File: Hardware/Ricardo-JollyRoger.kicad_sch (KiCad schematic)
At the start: 46 parts, among them J1 RBUS, J3 Conn_01x08_Pin, U1 ESP32-S3, U7 LM66200DRLR, Y1 R940000171

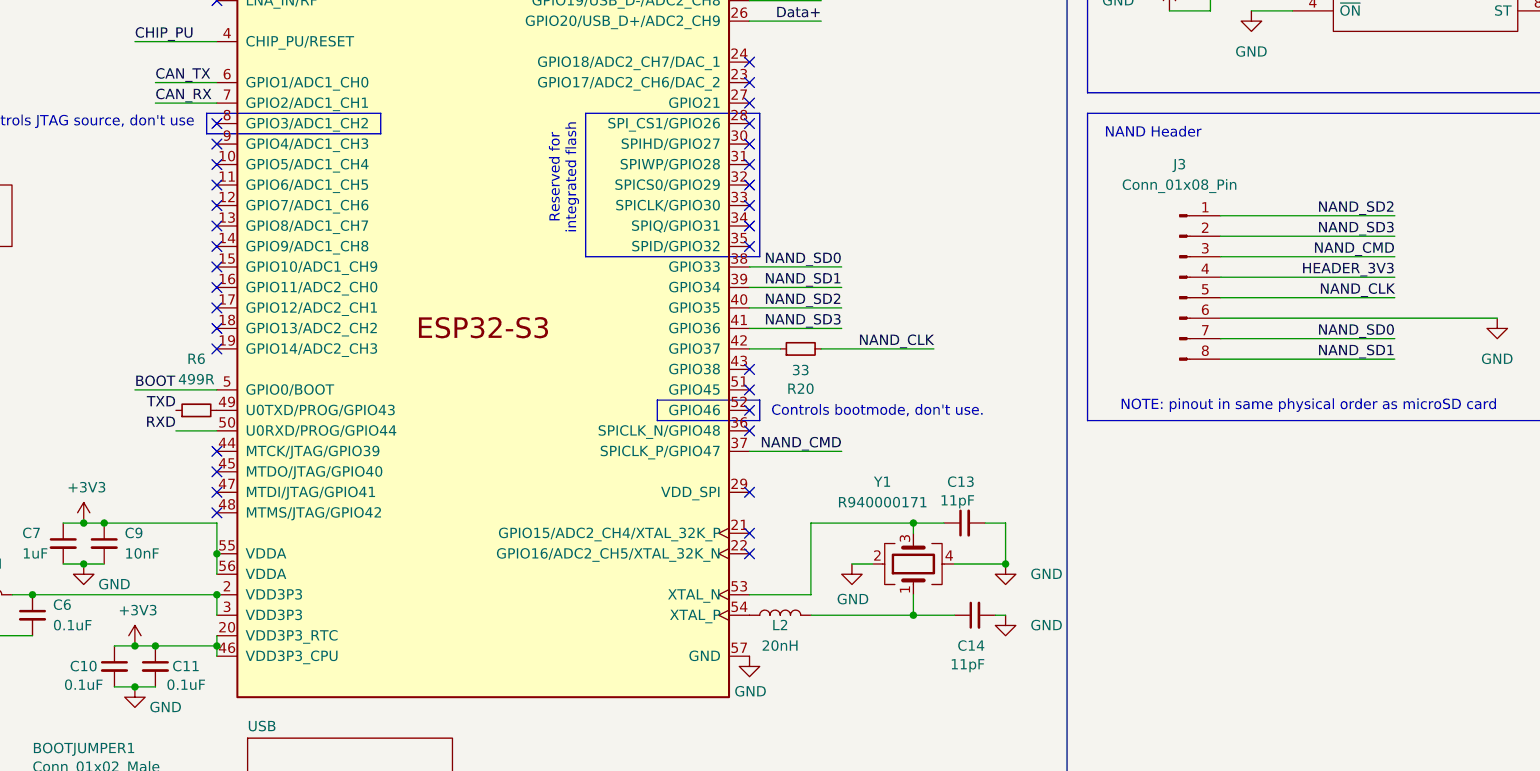
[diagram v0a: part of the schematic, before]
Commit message: Added GPIO breakout
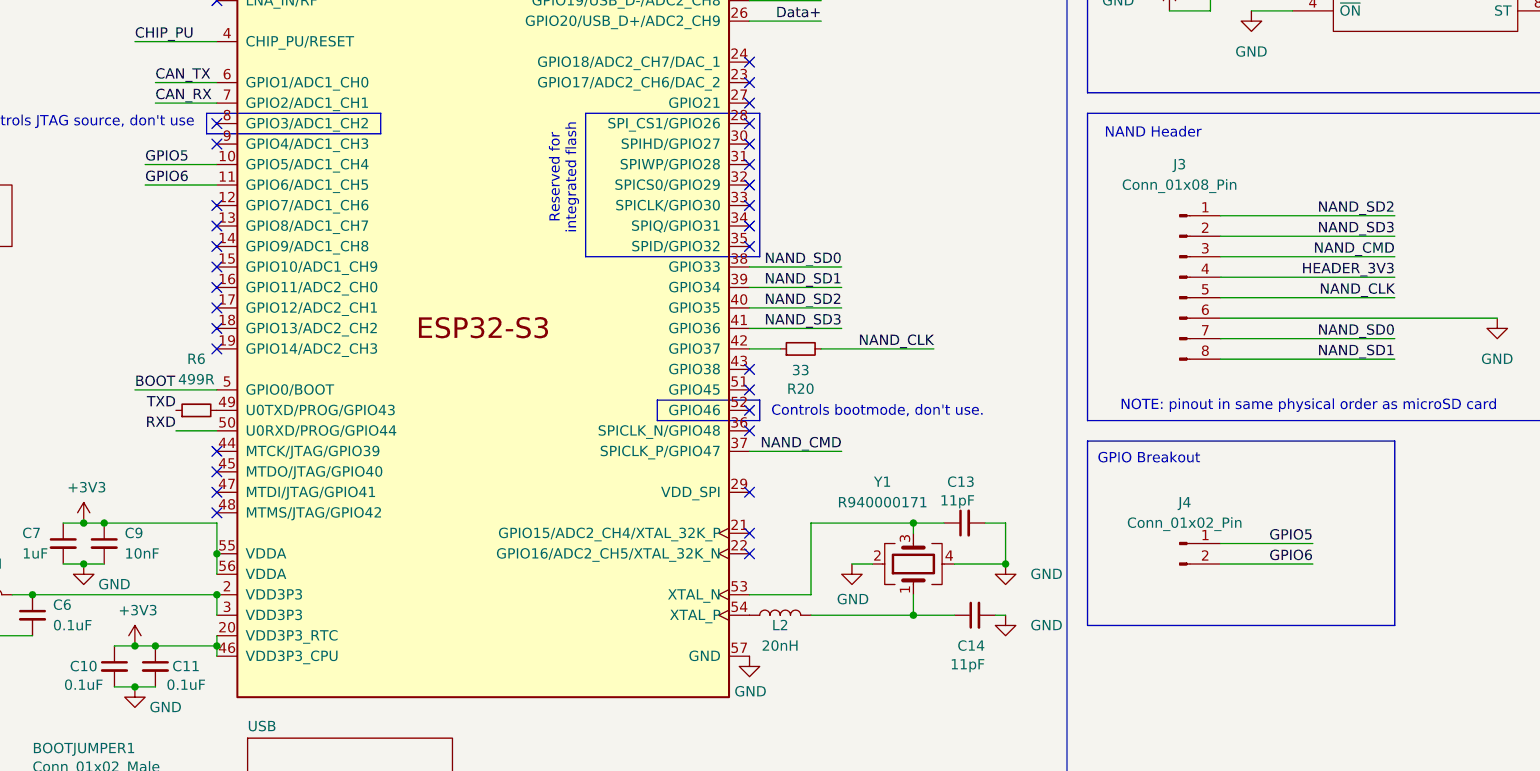
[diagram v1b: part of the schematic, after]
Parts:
- added J4: Conn_01x02_Pin, Connector_Molex:Molex_Pico-Clasp_202396-0207_1x02-1MP_P1.00mm_Horizontal, symbol Connector:Conn_01x02_Pin
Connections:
- net GPIO5: now reaches U1.10 (GPIO5/ADC1_CH4)
- net GPIO5: now also J4.1 (Pin_1)
- net GPIO6: now reaches U1.11 (GPIO6/ADC1_CH5)
- net GPIO6: now also J4.2 (Pin_2)
- no-connect marks 34 -> 32
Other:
- note added: "GPIO Breakout"
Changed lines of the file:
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@@
 	)
 	(no_connect
-		(at 69.85 82.55)
-	)
-	(no_connect
 		(at 135.89 87.63)
 	)
@@
 	)
 	(no_connect
-		(at 69.85 85.09)
-	)
-	(no_connect
 		(at 135.89 72.39)
 	)
@@
 	(wire
 		(pts
+			(xy 60.96 82.55) (xy 69.85 82.55)
+		)
+		(stroke
+			(width 0)
+			(type default)
+		)
+	)
+	(wire
+		(pts
 			(xy 30.48 182.88) (xy 30.48 185.42)
 		)
@@
 	(wire
 		(pts
+			(xy 60.96 85.09) (xy 69.85 85.09)
+		)
+		(stroke
+			(width 0)
+			(type default)
+		)
+	)
+	(wire
+		(pts
 			(xy 156.21 127) (xy 156.21 128.27)
 		)
@@
 		)
 	)
+	(wire
+		(pts
+			(xy 194.31 129.54) (xy 205.74 129.54)
+		)
+		(stroke
+			(width 0)
+			(type default)
+		)
+	)
 	(polyline
 		(pts
@@
 	(wire
 		(pts
+			(xy 194.31 132.08) (xy 205.74 132.08)
+		)
+		(stroke
+			(width 0)
+			(type default)
+		)
+	)
+	(wire
+		(pts
 			(xy 13.97 40.64) (xy 22.86 40.64)
 		)
@@
 		)
 	)
+	(rectangle
+		(start 177.8 116.84)
+		(end 215.9 139.7)
+		(stroke
+			(width 0)
+			(type default)
+		)
+		(fill
+			(type none)
+		)
+	)
 	(text "Controls bootmode, don't use.\n"
 		(exclude_from_sim no)
@@
 		)
 	)
+	(text "GPIO Breakout"
+		(exclude_from_sim no)
+		(at 185.42 119.126 0)
+		(effects
+			(font
+				(size 1.27 1.27)
+			)
+		)
+	)
 	(text "Controls JTAG source, don't use\n"
 		(exclude_from_sim no)
@@
 		)
 	)
+	(label "GPIO6"
+		(at 205.74 132.08 180)
+		(fields_autoplaced yes)
+		(effects
+			(font
+				(size 1.27 1.27)
+			)
+			(justify right bottom)
+		)
+	)
 	(label "CAN_TX"
 		(at 13.97 30.48 0)
@@
 		)
 	)
+	(label "GPIO5"
+		(at 60.96 82.55 0)
+		(fields_autoplaced yes)
+		(effects
+			(font
+				(size 1.27 1.27)
+			)
+			(justify left bottom)
+		)
+	)
 	(label "NAND_SD0"
 		(at 222.25 31.75 180)
@@
 		)
 	)
+	(label "GPIO5"
+		(at 205.74 129.54 180)
+		(fields_autoplaced yes)
+		(effects
+			(font
+				(size 1.27 1.27)
+			)
+			(justify right bottom)
+		)
+	)
 	(label "CAN-"
 		(at 115.57 187.96 0)
@@
 		)
 	)
+	(label "GPIO6"
+		(at 60.96 85.09 0)
+		(fields_autoplaced yes)
+		(effects
+			(font
+				(size 1.27 1.27)
+			)
+			(justify left bottom)
+		)
+	)
 	(label "TXD"
 		(at 17.78 21.59 0)
@@
 					(unit 1)
 				)
+			)
+		)
+	)
+	(symbol
+		(lib_id "Connector:Conn_01x02_Pin")
+		(at 189.23 129.54 0)
+		(unit 1)
+		(exclude_from_sim no)
+		(in_bom yes)
+		(on_board yes)
+		(dnp no)
+		(fields_autoplaced yes)
+		(property "Reference" "J4"
+			(at 189.865 124.46 0)
+			(effects
+				(font
+					(size 1.27 1.27)
+				)
+			)
+		)
+		(property "Value" "Conn_01x02_Pin"
+			(at 189.865 127 0)
+			(effects
+				(font
+					(size 1.27 1.27)
+				)
+			)
+		)
+		(property "Footprint" "Connector_Molex:Molex_Pico-Clasp_202396-0207_1x02-1MP_P1.00mm_Horizontal"
+			(at 189.23 129.54 0)
+			(effects
+				(font
+					(size 1.27 1.27)
+				)
+				(hide yes)
+			)
+		)
+		(property "Datasheet" "~"
+			(at 189.23 129.54 0)
+			(effects
+				(font
+					(size 1.27 1.27)
+				)
+				(hide yes)
+			)
+		)
+		(property "Description" "Generic connector, single row, 01x02, script generated"
+			(at 189.23 129.54 0)
+			(effects
+				(font
+					(size 1.27 1.27)
+				)
+				(hide yes)
+			)
+		)
+		(pin "2"
+		)
+		(pin "1"
+		)
+		(instances
+			(project ""
+				(path "/7db990e4-92e1-4f99-b4d2-435bbec1ba83"
+					(reference "J4")
+					(unit 1)
+				)

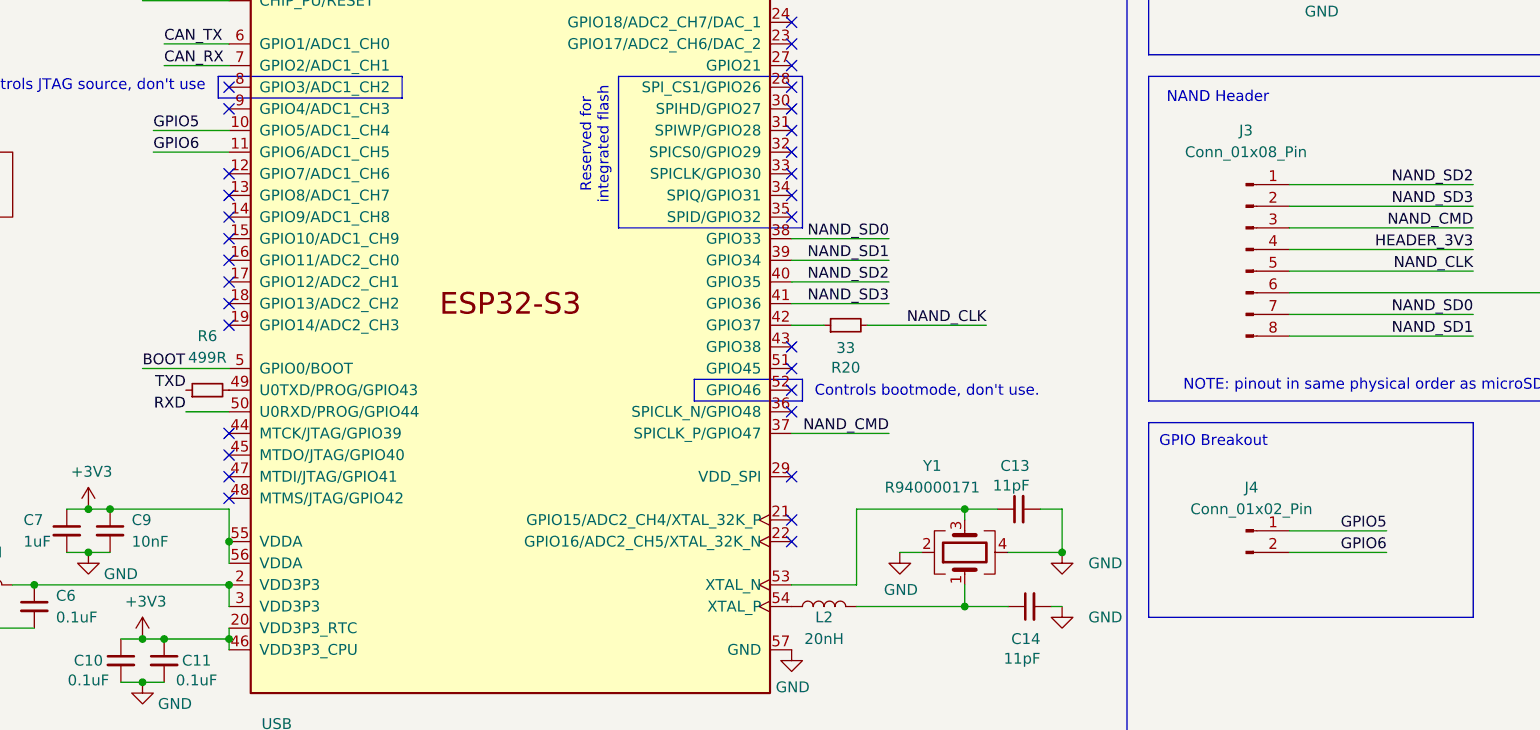
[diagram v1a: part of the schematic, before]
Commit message: Upgrade GPIO breakout to four pins
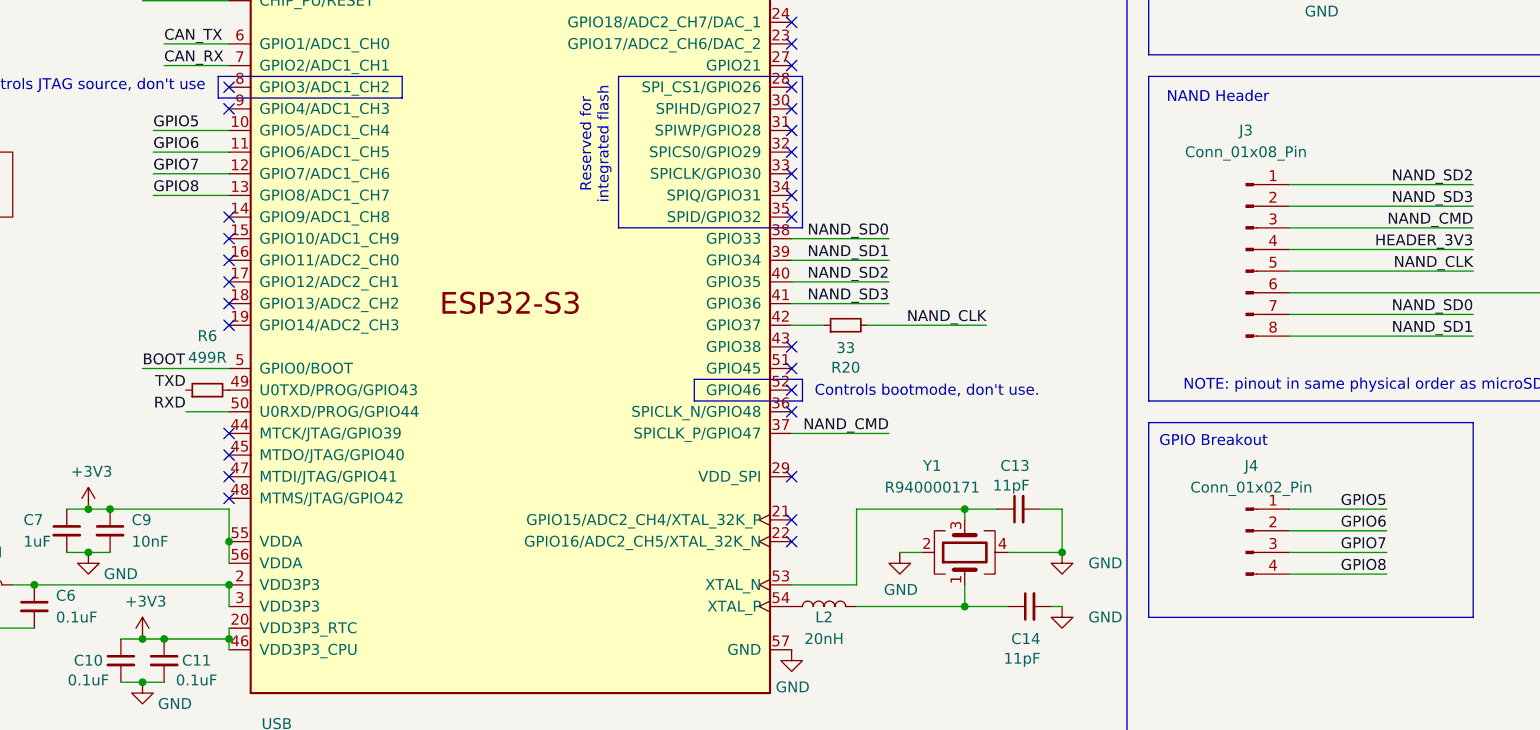
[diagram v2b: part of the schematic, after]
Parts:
- J4: footprint Connector_Molex:Molex_Pico-Clasp_202396-0207_1x02-1MP_P1.00mm_Horizontal -> Connector_Molex:Molex_Pico-Clasp_202396-0407_1x04-1MP_P1.00mm_Horizontal; symbol Connector:Conn_01x02_Pin -> Connector:Conn_01x04_Pin
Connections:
- net GPIO7: now reaches U1.12 (GPIO7/ADC1_CH6)
- net GPIO7: now also J4.3 (Pin_3)
- net GPIO8: now reaches U1.13 (GPIO8/ADC1_CH7)
- net GPIO8: now also J4.4 (Pin_4)
- no-connect marks 32 -> 30
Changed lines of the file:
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@@
 	)
 	(no_connect
-		(at 69.85 87.63)
-	)
-	(no_connect
 		(at 135.89 87.63)
 	)
@@
 	)
 	(no_connect
-		(at 69.85 90.17)
-	)
-	(no_connect
 		(at 135.89 69.85)
 	)
@@
 		)
 	)
+	(wire
+		(pts
+			(xy 194.31 134.62) (xy 205.74 134.62)
+		)
+		(stroke
+			(width 0)
+			(type default)
+		)
+	)
 	(polyline
 		(pts
@@
 	(wire
 		(pts
+			(xy 60.96 87.63) (xy 69.85 87.63)
+		)
+		(stroke
+			(width 0)
+			(type default)
+		)
+	)
+	(wire
+		(pts
 			(xy 57.15 170.18) (xy 63.5 170.18)
 		)
@@
 	(wire
 		(pts
+			(xy 60.96 90.17) (xy 69.85 90.17)
+		)
+		(stroke
+			(width 0)
+			(type default)
+		)
+	)
+	(wire
+		(pts
 			(xy 161.29 132.08) (xy 167.64 132.08)
 		)
@@
 	(wire
 		(pts
-			(xy 194.31 129.54) (xy 205.74 129.54)
+			(xy 194.31 127) (xy 205.74 127)
 		)
 		(stroke
@@
 	(wire
 		(pts
-			(xy 194.31 132.08) (xy 205.74 132.08)
+			(xy 194.31 129.54) (xy 205.74 129.54)
 		)
 		(stroke
@@
 	(wire
 		(pts
+			(xy 194.31 132.08) (xy 205.74 132.08)
+		)
+		(stroke
+			(width 0)
+			(type default)
+		)
+	)
+	(wire
+		(pts
 			(xy 45.72 165.1) (xy 45.72 170.18)
 		)
@@
 		)
 	)
+	(label "GPIO8"
+		(at 60.96 90.17 0)
+		(fields_autoplaced yes)
+		(effects
+			(font
+				(size 1.27 1.27)
+			)
+			(justify left bottom)
+		)
+	)
 	(label "NAND_SD0"
 		(at 147.32 95.25 180)
@@
 		)
 	)
+	(label "GPIO8"
+		(at 205.74 134.62 180)
+		(fields_autoplaced yes)
+		(effects
+			(font
+				(size 1.27 1.27)
+			)
+			(justify right bottom)
+		)
+	)
 	(label "CAN+"
 		(at 115.57 185.42 0)
@@
 		)
 	)
+	(label "GPIO7"
+		(at 60.96 87.63 0)
+		(fields_autoplaced yes)
+		(effects
+			(font
+				(size 1.27 1.27)
+			)
+			(justify left bottom)
+		)
+	)
 	(label "BOOT"
 		(at 53.34 191.77 180)
@@
 		)
 	)
+	(label "GPIO7"
+		(at 205.74 132.08 180)
+		(fields_autoplaced yes)
+		(effects
+			(font
+				(size 1.27 1.27)
+			)
+			(justify right bottom)
+		)
+	)
 	(label "NAND_CLK"
 		(at 215.9 99.06 180)
@@
 	)
 	(label "GPIO6"
-		(at 205.74 132.08 180)
+		(at 205.74 129.54 180)
 		(fields_autoplaced yes)
 		(effects
@@
 	)
 	(label "GPIO5"
-		(at 205.74 129.54 180)
+		(at 205.74 127 180)
 		(fields_autoplaced yes)
 		(effects
@@
 	)
 	(symbol
-		(lib_id "Connector:Conn_01x02_Pin")
+		(lib_id "Connector:Conn_01x04_Pin")
 		(at 189.23 129.54 0)
 		(unit 1)
@@
 		(fields_autoplaced yes)
 		(property "Reference" "J4"
-			(at 189.865 124.46 0)
+			(at 189.865 121.92 0)
 			(effects
 				(font
@@
 		)
 		(property "Value" "Conn_01x02_Pin"
-			(at 189.865 127 0)
+			(at 189.865 124.46 0)
 			(effects
 				(font
@@
 			)
 		)
-		(property "Footprint" "Connector_Molex:Molex_Pico-Clasp_202396-0207_1x02-1MP_P1.00mm_Horizontal"
+		(property "Footprint" "Connector_Molex:Molex_Pico-Clasp_202396-0407_1x04-1MP_P1.00mm_Horizontal"
 			(at 189.23 129.54 0)
 			(effects
@@
 			)
 		)
-		(property "Description" "Generic connector, single row, 01x02, script generated"
+		(property "Description" "Generic connector, single row, 01x04, script generated"
 			(at 189.23 129.54 0)
 			(effects
@@
 		(pin "1"
 		)
+		(pin "4"
+		)
+		(pin "3"
+		)
 		(instances

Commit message: Added 3V3 and GND to GPIO breakout
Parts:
- J4: value Conn_01x02_Pin -> Conn_01x06_Pin; footprint Connector_Molex:Molex_Pico-Clasp_202396-0407_1x04-1MP_P1.00mm_Horizontal -> Connector_Molex:Molex_Pico-Clasp_202396-0607_1x06-1MP_P1.00mm_Horizontal; symbol Connector:Conn_01x04_Pin -> Connector:Conn_01x06_Pin
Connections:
- net +3V3: now also J4.5 (Pin_5)
- net GND: now also J4.6 (Pin_6)

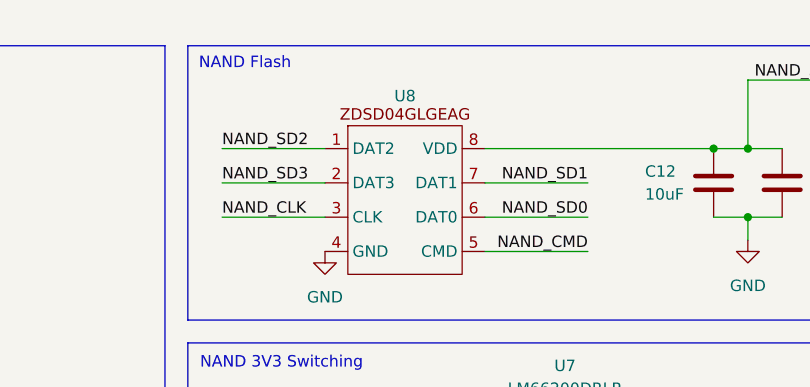
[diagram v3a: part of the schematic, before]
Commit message: Updated NAND flash symbol
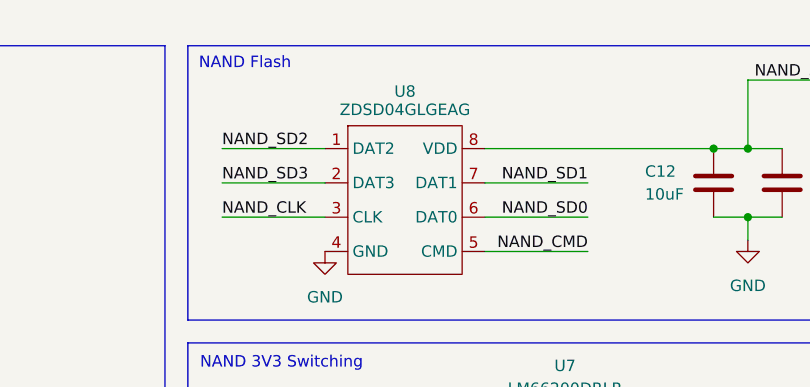
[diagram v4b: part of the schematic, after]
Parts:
- U8: value ~ -> ZDSD04GLGEAG
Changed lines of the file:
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@@
 		(dnp no)
 		(property "Reference" "U8"
-			(at 201.93 18.288 0)
+			(at 201.93 17.78 0)
 			(effects
 				(font
@@
 			)
 		)
-		(property "Value" "~"
-			(at 201.93 20.32 0)
+		(property "Value" "ZDSD04GLGEAG"
+			(at 201.93 19.812 0)
 			(effects
 				(font
@@
 			)
 		)
-		(property "Datasheet" ""
+		(property "Datasheet" "https://www.lcsc.com/datasheet/lcsc_datasheet_2410010101_Zetta-ZDSD04GLGEAG_C2875854.pdf"
 			(at 201.93 21.59 0)
 			(effects

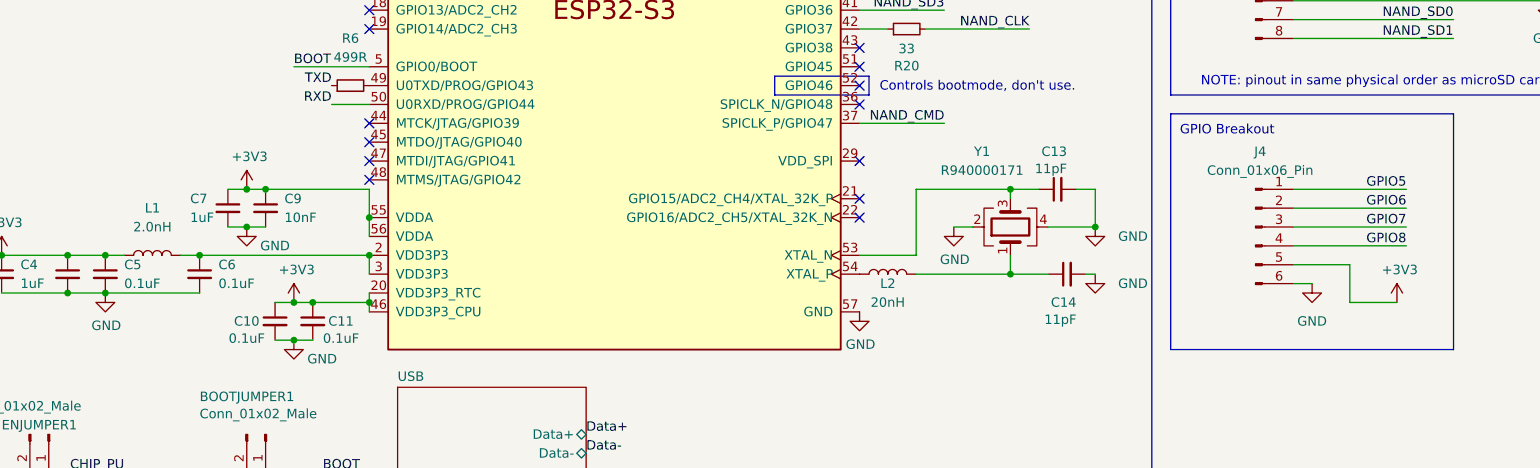
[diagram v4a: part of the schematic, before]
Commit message: Changed GPIO breakout to 8 pin connector
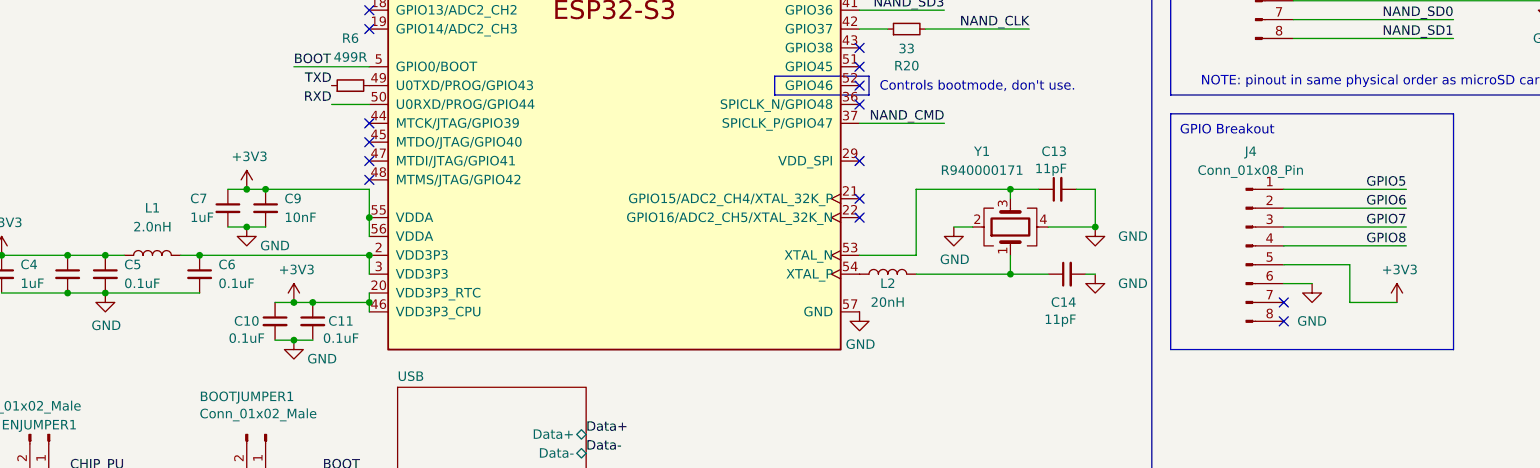
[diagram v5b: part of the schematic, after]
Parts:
- J4: value Conn_01x06_Pin -> Conn_01x08_Pin; footprint Connector_Molex:Molex_Pico-Clasp_202396-0607_1x06-1MP_P1.00mm_Horizontal -> Connector_Molex:Molex_Pico-Clasp_202396-0807_1x08-1MP_P1.00mm_Horizontal; symbol Connector:Conn_01x06_Pin -> Connector:Conn_01x08_Pin
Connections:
- no-connect marks 30 -> 32
